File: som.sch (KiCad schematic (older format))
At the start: 39 parts, among them T2 BSS138APW, T4 BSS138APW, T5 BSS138APW

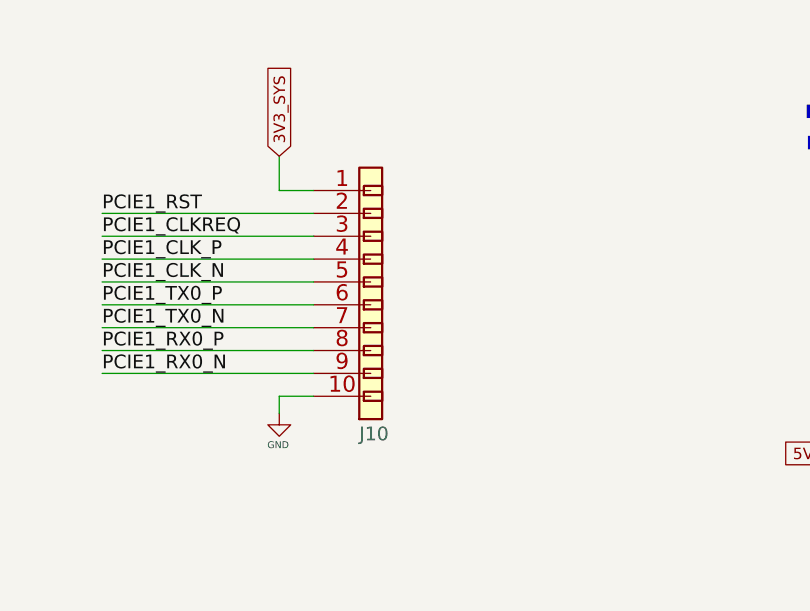
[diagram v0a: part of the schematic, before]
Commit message: Change J10 to 5051101097
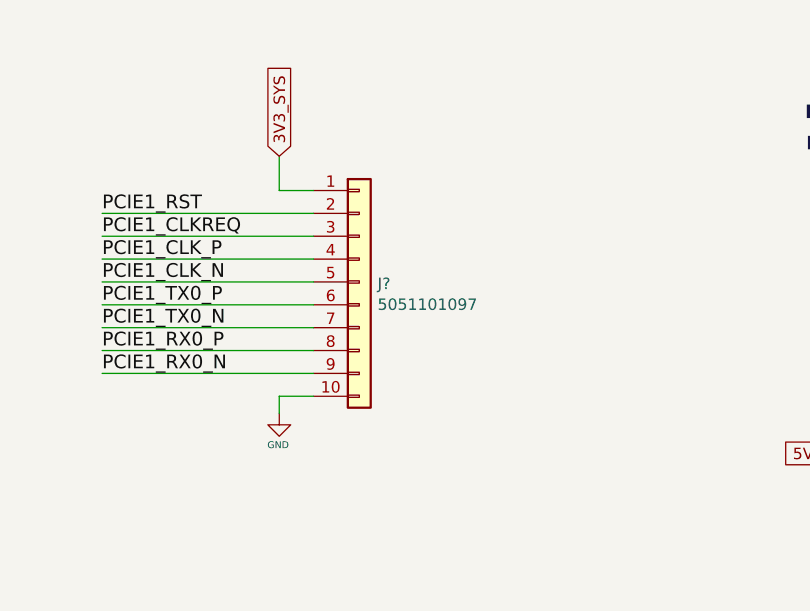
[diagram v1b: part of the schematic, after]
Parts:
- removed J10: ~, jetson-nano-baseboard-footprints:PCA-10, symbol jetson-nano-baseboard:ADAM-TECH_PCA-10
- added J?: 5051101097, jetson-nano-baseboard-footprints:5051101097, symbol jetson-nano-baseboard:5051101097
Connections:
- net 3V3_SYS: now also J?.1 (Pin_1)
- net GND: now also J?.10 (Pin_10)
- net PCIE1_CLKREQ: now also J?.3 (Pin_3)
- net PCIE1_CLK_N: now also J?.5 (Pin_5)
- net PCIE1_CLK_P: now also J?.4 (Pin_4)
- net PCIE1_RST: now also J?.2 (Pin_2)
- net PCIE1_RX0_N: now also J?.9 (Pin_9)
- net PCIE1_RX0_P: now also J?.8 (Pin_8)
- net PCIE1_TX0_N: now also J?.7 (Pin_7)
- net PCIE1_TX0_P: now also J?.6 (Pin_6)
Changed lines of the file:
@@
-$EndComp
-$Comp
-L jetson-nano-baseboard:ADAM-TECH_PCA-10 J10
-U 1 1 5E7103EF
-P 11650 1675
-F 0 "J10" H 11650 975 60  0000 L BNN
-F 1 "~" H 11650 1675 50  0001 C CNN
-F 2 "jetson-nano-baseboard-footprints:PCA-10" H 11650 1675 50  0001 C CNN
-F 3 "" H 11650 1675 50  0001 C CNN
-F 4 "PCA-10" H -9930 -4187 50  0001 C CNN "MPN"
-F 5 "Adam Tech" H -9930 -4187 50  0001 C CNN "Manufacturer"
-	1    11650 1675
-	1    0    0    -1
 $EndComp
 $Comp
@@
 	1    0    0    -1
 $EndComp
+$Comp
+L jetson-nano-baseboard:5051101097 J?
+U 1 1 62043EB3
+P 11650 2275
+F 0 "J?" H 11730 2867 50  0000 L CNN
+F 1 "5051101097" H 11730 2776 50  0000 L CNN
+F 2 "jetson-nano-baseboard-footprints:5051101097" H 11500 2025 50  0001 C CNN
+F 3 "" H 11200 1975 50  0001 C CNN
+F 4 "5051101097" H 11350 1875 60  0001 L CNN "MPN"
+F 5 "Molex" H 11200 2125 60  0001 L CNN "Manufacturer"
+	1    11650 2275
+	1    0    0    -1
+$EndComp

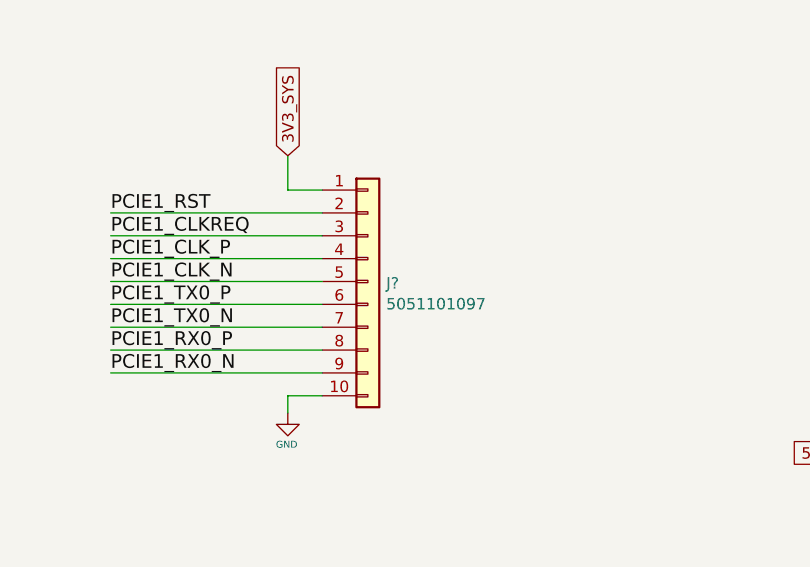
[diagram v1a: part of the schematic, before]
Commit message: Fix annotation on J10
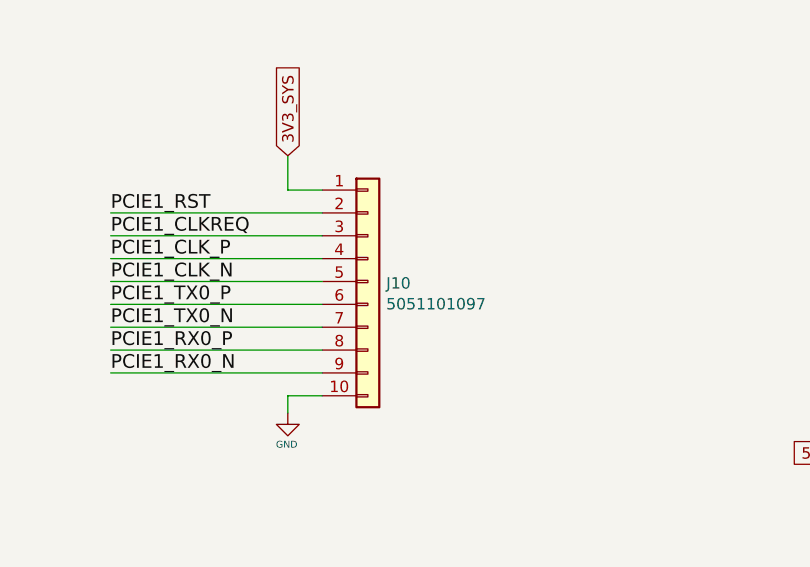
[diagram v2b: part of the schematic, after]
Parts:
- gave numbers to parts that had none: 1
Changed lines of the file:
@@
 $EndComp
 $Comp
-L jetson-nano-baseboard:5051101097 J?
+L jetson-nano-baseboard:5051101097 J10
 U 1 1 62043EB3
 P 11650 2275
-F 0 "J?" H 11730 2867 50  0000 L CNN
+F 0 "J10" H 11730 2867 50  0000 L CNN
 F 1 "5051101097" H 11730 2776 50  0000 L CNN
 F 2 "jetson-nano-baseboard-footprints:5051101097" H 11500 2025 50  0001 C CNN
